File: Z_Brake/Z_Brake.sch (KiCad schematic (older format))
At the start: 29 parts, among them K1 EC2-24NU, K2 EC2-24NU, P1 CONN_01X04, P2 CONN_01X02, P3 CONN_01X04, P4 CONN_01X04, Q1 2N7002, U1 LM397

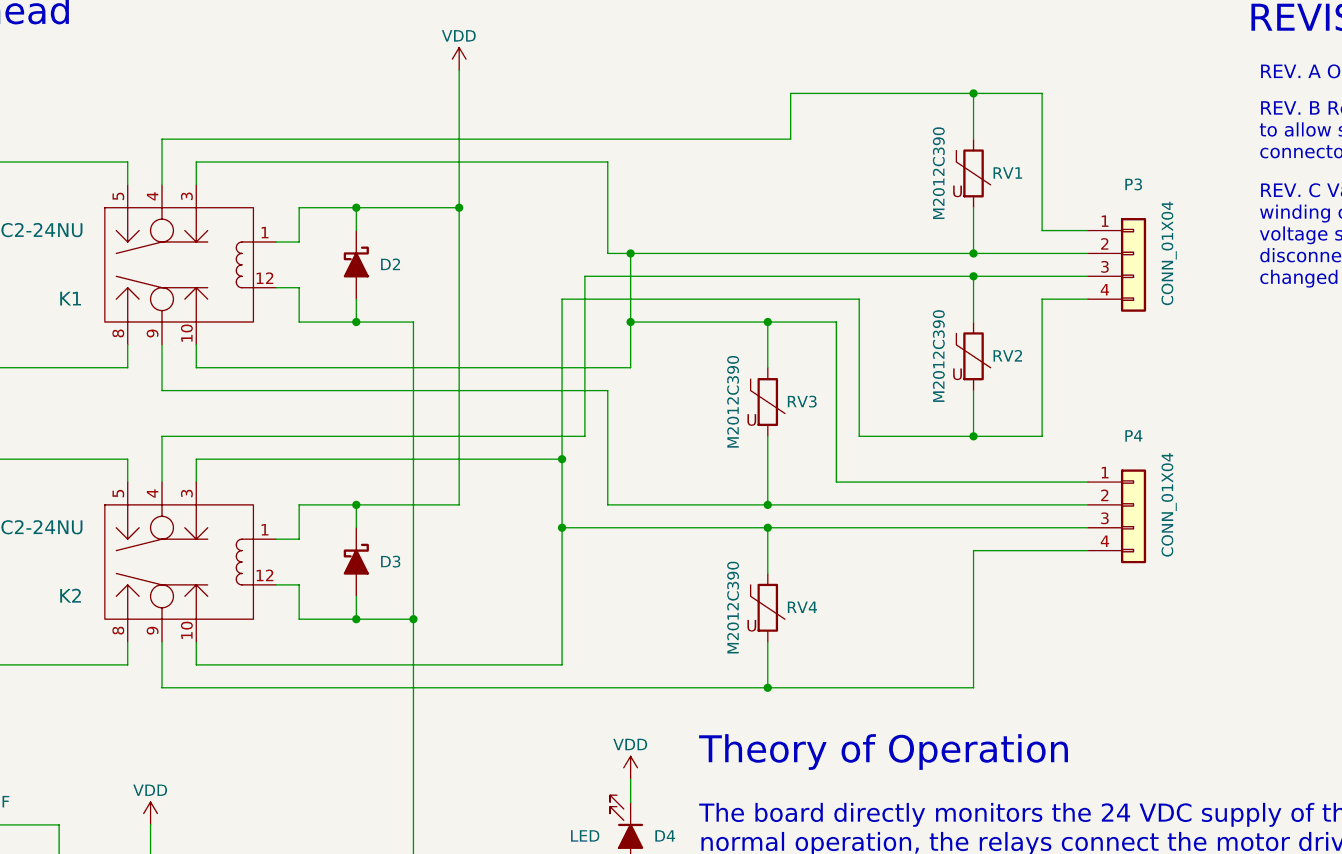
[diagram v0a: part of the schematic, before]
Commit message: Converted to single motor output
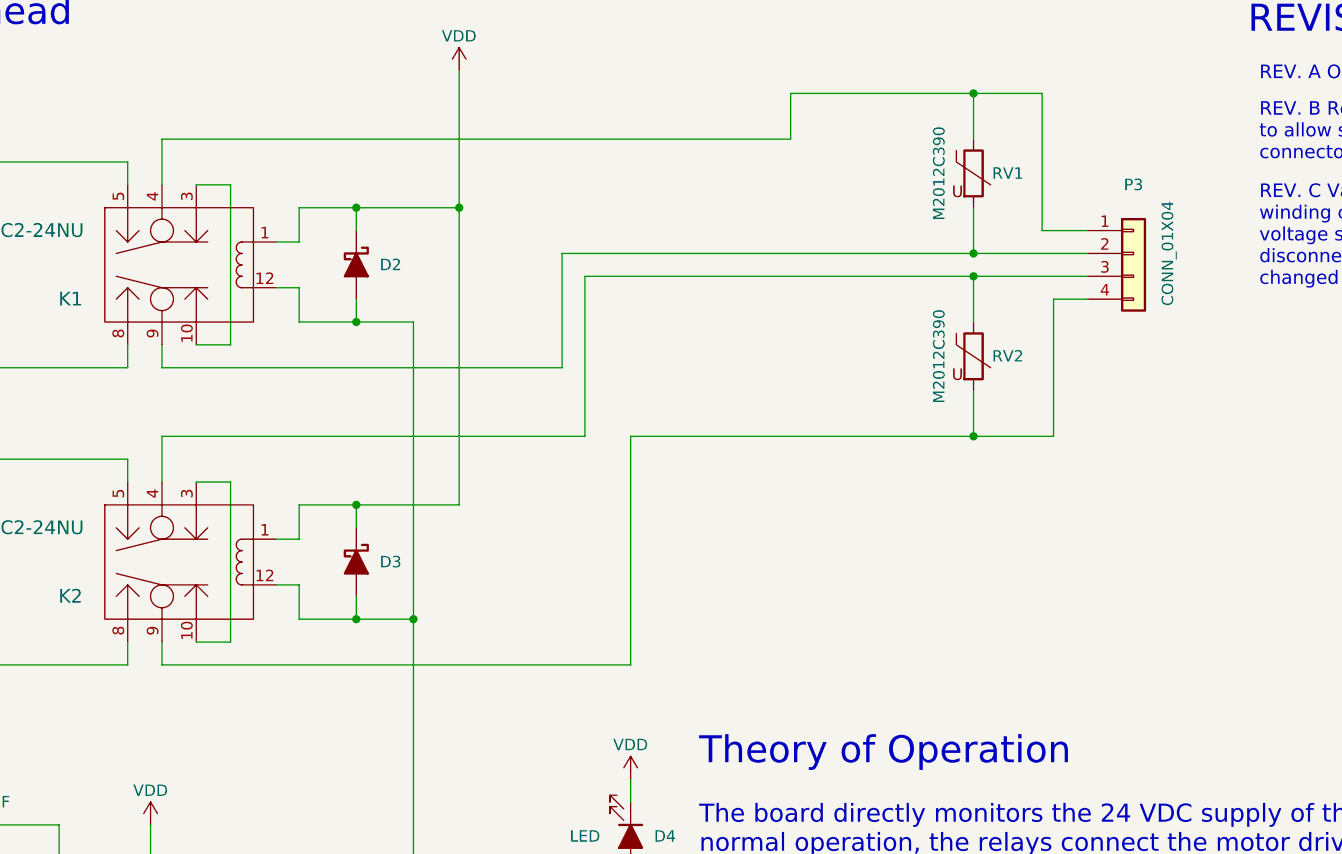
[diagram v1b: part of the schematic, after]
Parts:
- removed P4: CONN_01X04, Pin_Headers:Pin_Header_Straight_1x04, symbol Connector_Generic:Conn_01x04
- removed RV3, RV4: M2012C390, Resistors_SMD:R_0805, symbol Device:Varistor
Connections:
- net at K1.10, K1.3: no longer P3.2 (Pin_2), RV1.2
- net at K1.9: now also P3.2 (Pin_2), RV1.2
- net at K2.10, K2.3: no longer P3.4 (Pin_4), RV2.2
- net at K2.9: now also P3.4 (Pin_4), RV2.2
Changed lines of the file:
@@
-$EndComp
-$Comp
-L ec2-24nu:EC2-24NU K1
-U 1 1 5A25BAB4
-P 4450 1950
-F 0 "K1" H 4050 1800 60  0000 C CNN
-F 1 "EC2-24NU" H 3900 2100 60  0000 C CNN
-F 2 "AO Parts:EC2_Relay" H 4200 1450 60  0001 C CNN
-F 3 "" H 4200 1450 60  0001 C CNN
-F 4 "EC2-24NU" H 4450 1950 60  0001 C CNN "Part Number"
-F 5 "Digikey" H 4450 1950 60  0001 C CNN "Primary Supplier"
-F 6 "399-11037-5-ND" H 4450 1950 60  0001 C CNN "DKPN"
-F 7 "EL-MS-0492" H 4450 1950 60  0001 C CNN "AO Part Number"
-	1    4450 1950
-	1    0    0    -1
 $EndComp
 $Comp
@@
 	1    0    0    -1
 $EndComp
-$Comp
-L Connector_Generic:Conn_01x04 P4
-U 1 1 5A25BDE2
-P 8700 3000
-F 0 "P4" H 8700 3300 50  0000 C CNN
-F 1 "CONN_01X04" V 8850 3000 50  0000 C CNN
-F 2 "Pin_Headers:Pin_Header_Straight_1x04" H 8700 3000 50  0001 C CNN
-F 3 "" H 8700 3000 50  0000 C CNN
-F 4 "WM4802-ND" H 8700 3000 50  0001 C CNN "DKPN"
-	1    8700 3000
-	1    0    0    -1
-$EndComp
 Wire Wire Line
 	4300 1600 4300 1500
@@
 	4450 1400 7200 1400
 Wire Wire Line
-	6400 1900 6400 1500
-Wire Wire Line
-	6400 1500 4600 1500
-Wire Wire Line
-	4600 1500 4600 1600
-Connection ~ 6500 1900
-Wire Wire Line
-	4450 2300 4450 2500
-Wire Wire Line
-	4450 2500 6400 2500
-Wire Wire Line
-	6400 2500 6400 3000
-Wire Wire Line
-	6400 3000 7100 3000
-Wire Wire Line
-	4600 2300 4600 2400
-Wire Wire Line
-	6500 2400 4600 2400
-Wire Wire Line
 	6300 2000 6300 2700
 Wire Wire Line
@@
 Wire Wire Line
 	4450 2700 4450 2900
-Wire Wire Line
-	4450 3600 4450 3800
-Wire Wire Line
-	4450 3800 7100 3800
-Wire Wire Line
-	7100 3800 7100 3600
-Wire Wire Line
-	4600 3600 4600 3700
-Wire Wire Line
-	6200 3700 4600 3700
-Wire Wire Line
-	6200 2100 6200 2800
-Wire Wire Line
-	6200 3100 7100 3100
-Connection ~ 6200 3100
-Wire Wire Line
-	4600 2900 4600 2800
-Wire Wire Line
-	4600 2800 6200 2800
-Connection ~ 6200 2800
 $Comp
 L Device:D_Schottky_ALT D2
@@
 	1    0    0    -1
 $EndComp
-$Comp
-L Device:Varistor RV3
-U 1 1 5B281699
-P 7100 2550
-F 0 "RV3" H 7250 2550 50  0000 C CNN
-F 1 "M2012C390" V 6950 2550 50  0000 C CNN
-F 2 "Resistors_SMD:R_0805" V 7030 2550 50  0001 C CNN
-F 3 "" H 7100 2550 50  0000 C CNN
-F 4 "445-2549-1-ND" H 7100 2550 50  0001 C CNN "DKPN"
-	1    7100 2550
-	1    0    0    -1
-$EndComp
-Connection ~ 7100 3100
-Connection ~ 7100 3000
-$Comp
-L Device:Varistor RV4
-U 1 1 5B281A22
-P 7100 3450
-F 0 "RV4" H 7250 3450 50  0000 C CNN
-F 1 "M2012C390" V 6950 3450 50  0000 C CNN
-F 2 "Resistors_SMD:R_0805" V 7030 3450 50  0001 C CNN
-F 3 "" H 7100 3450 50  0000 C CNN
-F 4 "445-2549-1-ND" H 7100 3450 50  0001 C CNN "DKPN"
-	1    7100 3450
-	1    0    0    -1
-$EndComp
 Wire Wire Line
 	8500 1800 8300 1800
@@
 Connection ~ 8000 1200
 Wire Wire Line
-	6400 1900 6500 1900
-Wire Wire Line
 	8000 1700 8000 1900
-Connection ~ 8000 1900
 Wire Wire Line
 	6300 2000 8000 2000
@@
 Connection ~ 8000 2000
 Wire Wire Line
-	8500 2100 8300 2100
-Wire Wire Line
-	8300 2700 8300 2100
-Wire Wire Line
-	7500 2700 8000 2700
-Wire Wire Line
 	8000 2700 8000 2500
-Wire Wire Line
-	7500 2700 7500 2100
-Wire Wire Line
-	7500 2100 6200 2100
-Connection ~ 8000 2700
-Wire Wire Line
-	8500 2900 7400 2900
-Wire Wire Line
-	7400 2200 7400 2900
-Wire Wire Line
-	6500 2200 7100 2200
-Wire Wire Line
-	7100 2200 7100 2400
-Wire Wire Line
-	6500 1900 6500 2200
-Connection ~ 6500 2200
-Connection ~ 7100 2200
-Wire Wire Line
-	7100 2700 7100 3000
-Wire Wire Line
-	7100 3300 7100 3100
-Wire Wire Line
-	8500 3200 8000 3200
-Wire Wire Line
-	8000 3200 8000 3800
-Connection ~ 7100 3800
 Text Notes 8350 6950 0    118  ~ 0
 Z-BRAKE BOARD
@@
 C
 Wire Wire Line
-	6500 1900 8000 1900
-Wire Wire Line
-	6200 3100 6200 3700
-Wire Wire Line
-	6200 2800 6200 3100
-Wire Wire Line
 	5300 2200 5550 2200
 Wire Wire Line
@@
 	2100 3100 2250 3100
 Wire Wire Line
-	7100 3100 8500 3100
-Wire Wire Line
-	7100 3000 8500 3000
-Wire Wire Line
 	8000 1200 8300 1200
 Wire Wire Line
@@
 Wire Wire Line
 	8000 2000 8500 2000
-Wire Wire Line
-	8000 2700 8300 2700
-Wire Wire Line
-	6500 2200 6500 2400
-Wire Wire Line
-	7100 2200 7400 2200
-Wire Wire Line
-	7100 3800 8000 3800
 $Comp
 L Transistor_FET:2N7002 Q1
@@
 Wire Wire Line
 	5550 5700 5550 6650
+Wire Wire Line
+	2500 5400 2500 6000
+Wire Wire Line
+	2500 5200 2500 5400
+Connection ~ 2500 5400
+Wire Wire Line
+	3200 5400 2500 5400
+Wire Wire Line
+	2900 5600 3200 5600
+Connection ~ 2900 4700
+Wire Wire Line
+	2900 4700 2900 5600
+Connection ~ 2900 5600
+Wire Wire Line
+	1900 5600 1900 6000
+Wire Wire Line
+	1900 5200 1900 5600
+Connection ~ 1900 5600
+Wire Wire Line
+	1900 5600 2900 5600
+$Comp
+L power:VDD #PWR015
+U 1 1 5A6130DB
+P 3500 5150
+F 0 "#PWR015" H 3500 5000 50  0001 C CNN
+F 1 "VDD" H 3500 5300 50  0000 C CNN
+F 2 "" H 3500 5150 50  0000 C CNN
+F 3 "" H 3500 5150 50  0000 C CNN
+	1    3500 5150
+	1    0    0    -1
+$EndComp
+Wire Wire Line
+	3500 5150 3500 5250
+Wire Wire Line
+	3500 5750 3500 5900
+$Comp
+L power:GND #PWR08
+U 1 1 5A28666A
+P 3500 5900
+F 0 "#PWR08" H 3500 5650 50  0001 C CNN
+F 1 "GND" H 3500 5750 50  0000 C CNN
+F 2 "" H 3500 5900 50  0000 C CNN
+F 3 "" H 3500 5900 50  0000 C CNN
+	1    3500 5900
+	1    0    0    -1
+$EndComp
+$Comp
+L lm397:LM397 U1
+U 1 1 5A280FF5
+P 3450 5500
+F 0 "U1" H 3300 5200 60  0000 C CNN
+F 1 "LM397" H 3200 5800 60  0000 C CNN
+F 2 "TO_SOT_Packages_SMD:SOT-23-5" H 3500 5500 60  0001 C CNN
+F 3 "" H 3500 5500 60  0001 C CNN
+F 4 "LM397MF/NOPBCT-ND" H 3450 5500 50  0001 C CNN "DKPN"
+	1    3450 5500
+	1    0    0    -1
+$EndComp
+Wire Wire Line
+	4450 2300 4450 2400
+Wire Wire Line
+	4450 2400 6200 2400
+Wire Wire Line
+	6200 2400 6200 1900
+Wire Wire Line
+	6200 1900 8000 1900
+Connection ~ 8000 1900
+Wire Wire Line
+	4450 3600 4450 3700
+Wire Wire Line
+	4450 3700 6500 3700
+Wire Wire Line
+	6500 3700 6500 2700
+Wire Wire Line
+	6500 2700 8000 2700
+Wire Wire Line
+	8000 2700 8350 2700
+Wire Wire Line
+	8350 2700 8350 2100
+Wire Wire Line
+	8350 2100 8500 2100
+Connection ~ 8000 2700
+Wire Wire Line
+	4750 1600 4750 2300
+Wire Wire Line
+	4750 2900 4750 3600
+Wire Wire Line
+	4750 3600 4600 3600
+Wire Wire Line
+	4600 2900 4750 2900
+Wire Wire Line
+	4750 2300 4600 2300
+Wire Wire Line
+	4600 1600 4750 1600
+$Comp
+L ec2-24nu:EC2-24NU K1
+U 1 1 5A25BAB4
+P 4450 1950
+F 0 "K1" H 4050 1800 60  0000 C CNN
+F 1 "EC2-24NU" H 3900 2100 60  0000 C CNN
+F 2 "AO Parts:EC2_Relay" H 4200 1450 60  0001 C CNN
+F 3 "" H 4200 1450 60  0001 C CNN
+F 4 "EC2-24NU" H 4450 1950 60  0001 C CNN "Part Number"
+F 5 "Digikey" H 4450 1950 60  0001 C CNN "Primary Supplier"
+F 6 "399-11037-5-ND" H 4450 1950 60  0001 C CNN "DKPN"
+F 7 "EL-MS-0492" H 4450 1950 60  0001 C CNN "AO Part Number"
+	1    4450 1950
+	1    0    0    -1
+$EndComp
 $Comp
 L ec2-24nu:EC2-24NU K2
@@
 	1    0    0    -1
 $EndComp
-Wire Wire Line
-	2500 5400 2500 6000
-Wire Wire Line
-	2500 5200 2500 5400
-Connection ~ 2500 5400
-Wire Wire Line
-	3200 5400 2500 5400
-Wire Wire Line
-	2900 5600 3200 5600
-Connection ~ 2900 4700
-Wire Wire Line
-	2900 4700 2900 5600
-Connection ~ 2900 5600
-Wire Wire Line
-	1900 5600 1900 6000
-Wire Wire Line
-	1900 5200 1900 5600
-Connection ~ 1900 5600
-Wire Wire Line
-	1900 5600 2900 5600
-$Comp
-L power:VDD #PWR015
-U 1 1 5A6130DB
-P 3500 5150
-F 0 "#PWR015" H 3500 5000 50  0001 C CNN
-F 1 "VDD" H 3500 5300 50  0000 C CNN
-F 2 "" H 3500 5150 50  0000 C CNN
-F 3 "" H 3500 5150 50  0000 C CNN
-	1    3500 5150
-	1    0    0    -1
-$EndComp
-Wire Wire Line
-	3500 5150 3500 5250
-Wire Wire Line
-	3500 5750 3500 5900
-$Comp
-L power:GND #PWR08
-U 1 1 5A28666A
-P 3500 5900
-F 0 "#PWR08" H 3500 5650 50  0001 C CNN
-F 1 "GND" H 3500 5750 50  0000 C CNN
-F 2 "" H 3500 5900 50  0000 C CNN
-F 3 "" H 3500 5900 50  0000 C CNN
-	1    3500 5900
-	1    0    0    -1
-$EndComp
-$Comp
-L lm397:LM397 U1
-U 1 1 5A280FF5
-P 3450 5500
-F 0 "U1" H 3300 5200 60  0000 C CNN
-F 1 "LM397" H 3200 5800 60  0000 C CNN
-F 2 "TO_SOT_Packages_SMD:SOT-23-5" H 3500 5500 60  0001 C CNN
-F 3 "" H 3500 5500 60  0001 C CNN
-F 4 "LM397MF/NOPBCT-ND" H 3450 5500 50  0001 C CNN "DKPN"
-	1    3450 5500
-	1    0    0    -1
-$EndComp

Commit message: Starting on PCB layout
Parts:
- C1: footprint Capacitors_SMD:C_0603_HandSoldering -> Capacitor_SMD:C_0603_1608Metric_Pad1.08x0.95mm_HandSolder
- D1, D5: footprint Diodes_SMD:SMA_Handsoldering -> Diode_SMD:D_SMA_Handsoldering
- D2, D3: footprint Diodes_SMD:SOD-123 -> Diode_SMD:D_SOD-123
- D4: footprint Capacitors_SMD:C_0603_HandSoldering -> LED_SMD:LED_0603_1608Metric_Pad1.05x0.95mm_HandSolder
- K1: footprint AO Parts:EC2_Relay -> ec2:EC2_Relay; AO Part Number EL-MS-0492 -> (none)
- K2: footprint AO Parts:EC2_Relay -> ec2:EC2_Relay; AO Part Number EL-MS0492 -> (none)
- MH1, MH2, MH3, MH4: footprint AO Parts:MOUNT_HOLE -> MountingHole:MountingHole_2.5mm_Pad
- P1, P3: footprint Pin_Headers:Pin_Header_Straight_1x04 -> Molex:Molex-70543-0038-0-0-MFG
- P2: footprint Pin_Headers:Pin_Header_Straight_1x02 -> Molex:MOLEX_0705430001
- Q1: footprint TO_SOT_Packages_SMD:SOT-23 -> Package_TO_SOT_SMD:SOT-23_Handsoldering
- R1, R2, R3, R4, R5, R6, R7: footprint Resistors_SMD:R_0603_HandSoldering -> Resistor_SMD:R_0603_1608Metric_Pad0.98x0.95mm_HandSolder
- RV1, RV2: footprint Resistors_SMD:R_0805 -> Resistor_SMD:R_0805_2012Metric_Pad1.20x1.40mm_HandSolder
- U1: footprint TO_SOT_Packages_SMD:SOT-23-5 -> Package_TO_SOT_SMD:SOT-23-5_HandSoldering
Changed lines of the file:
@@
 F 0 "C1" V 3350 4200 50  0000 L CNN
 F 1 "0.22uF" V 3350 4500 50  0000 L CNN
-F 2 "Capacitors_SMD:C_0603_HandSoldering" H 3488 4250 50  0001 C CNN
+F 2 "Capacitor_SMD:C_0603_1608Metric_Pad1.08x0.95mm_HandSolder" H 3488 4250 50  0001 C CNN
 F 3 "" H 3450 4400 50  0000 C CNN
 F 4 "1276-6600-1-ND" V 3450 4400 50  0001 C CNN "DKPN"
@@
 F 0 "D1" V 2500 6300 50  0000 C CNN
 F 1 "10.0 V ZENER" H 2500 6000 50  0000 C CNN
-F 2 "Diodes_SMD:SMA_Handsoldering" H 2500 6150 50  0001 C CNN
+F 2 "Diode_SMD:D_SMA_Handsoldering" H 2500 6150 50  0001 C CNN
 F 3 "" H 2500 6150 50  0000 C CNN
 F 4 "SMAZ10-13-F" H 2500 6150 60  0001 C CNN "Part Number"
@@
 F 0 "P1" H 1400 2200 50  0000 C CNN
 F 1 "CONN_01X04" V 1550 1900 50  0000 C CNN
-F 2 "Pin_Headers:Pin_Header_Straight_1x04" H 1400 1900 50  0001 C CNN
+F 2 "Molex:Molex-70543-0038-0-0-MFG" H 1400 1900 50  0001 C CNN
 F 3 "" H 1400 1900 50  0000 C CNN
 F 4 "WM4802-ND" H 1400 1900 50  0001 C CNN "DKPN"
@@
 F 0 "P3" H 8700 2200 50  0000 C CNN
 F 1 "CONN_01X04" V 8850 1900 50  0000 C CNN
-F 2 "Pin_Headers:Pin_Header_Straight_1x04" H 8700 1900 50  0001 C CNN
+F 2 "Molex:Molex-70543-0038-0-0-MFG" H 8700 1900 50  0001 C CNN
 F 3 "" H 8700 1900 50  0000 C CNN
 F 4 "WM4802-ND" H 8700 1900 50  0001 C CNN "DKPN"
@@
 F 0 "D2" V 5300 2100 50  0000 C CNN
 F 1 "D_Schottky_ALT" H 5300 1850 50  0001 C CNN
-F 2 "Diodes_SMD:SOD-123" H 5300 1950 50  0001 C CNN
+F 2 "Diode_SMD:D_SOD-123" H 5300 1950 50  0001 C CNN
 F 3 "" H 5300 1950 50  0000 C CNN
 F 4 "BAT48ZFILM" H 5300 1950 60  0001 C CNN "Part Number"
@@
 F 0 "D3" V 5300 3400 50  0000 C CNN
 F 1 "D_Schottky_ALT" H 5300 3150 50  0001 C CNN
-F 2 "Diodes_SMD:SOD-123" H 5300 3250 50  0001 C CNN
+F 2 "Diode_SMD:D_SOD-123" H 5300 3250 50  0001 C CNN
 F 3 "" H 5300 3250 50  0000 C CNN
 F 4 "BAT48ZFILM" H 5300 3250 60  0001 C CNN "Part Number"
@@
 F 0 "P2" H 1400 3000 50  0000 C CNN
 F 1 "CONN_01X02" V 1550 3200 50  0000 C CNN
-F 2 "Pin_Headers:Pin_Header_Straight_1x02" H 1400 3200 50  0001 C CNN
+F 2 "Molex:MOLEX_0705430001" H 1400 3200 50  0001 C CNN
 F 3 "" H 1400 3200 50  0000 C CNN
 F 4 "WM4800-ND" H 1400 3200 50  0001 C CNN "DKPN"
@@
 F 0 "D4" V 6500 4600 50  0000 C CNN
 F 1 "LED" V 6500 4250 50  0000 C CNN
-F 2 "Capacitors_SMD:C_0603_HandSoldering" H 6500 4450 50  0001 C CNN
+F 2 "LED_SMD:LED_0603_1608Metric_Pad1.05x0.95mm_HandSolder" H 6500 4450 50  0001 C CNN
 F 3 "" H 6500 4450 50  0000 C CNN
 F 4 "160-1184-1-ND" V 6500 4450 50  0001 C CNN "DKPN"
@@
 F 0 "R7" H 6650 4850 50  0000 C CNN
 F 1 "3.3k" H 6350 4850 50  0000 C CNN
-F 2 "Resistors_SMD:R_0603_HandSoldering" V 6430 4850 50  0001 C CNN
+F 2 "Resistor_SMD:R_0603_1608Metric_Pad0.98x0.95mm_HandSolder" V 6430 4850 50  0001 C CNN
 F 3 "" H 6500 4850 50  0000 C CNN
 F 4 "311-3.30KHRCT-ND" H 6500 4850 50  0001 C CNN "DKPN"
@@
 F 0 "R6" V 4930 5500 50  0000 C CNN
 F 1 "10k" V 4750 5500 50  0000 C CNN
-F 2 "Resistors_SMD:R_0603_HandSoldering" V 4780 5500 50  0001 C CNN
+F 2 "Resistor_SMD:R_0603_1608Metric_Pad0.98x0.95mm_HandSolder" V 4780 5500 50  0001 C CNN
 F 3 "" H 4850 5500 50  0000 C CNN
 F 4 "311-10.0KHRCT-ND" V 4850 5500 50  0001 C CNN "DKPN"
@@
 F 0 "R4" V 3530 4700 50  0000 C CNN
 F 1 "180k" V 3350 4700 50  0000 C CNN
-F 2 "Resistors_SMD:R_0603_HandSoldering" V 3380 4700 50  0001 C CNN
+F 2 "Resistor_SMD:R_0603_1608Metric_Pad0.98x0.95mm_HandSolder" V 3380 4700 50  0001 C CNN
 F 3 "" H 3450 4700 50  0001 C CNN
 F 4 "311-180KHRCT-ND" V 3450 4700 50  0001 C CNN "DKPN"
@@
 F 0 "R3" H 2650 5050 50  0000 C CNN
 F 1 "10k" H 2300 5050 50  0000 C CNN
-F 2 "Resistors_SMD:R_0603_HandSoldering" V 2430 5050 50  0001 C CNN
+F 2 "Resistor_SMD:R_0603_1608Metric_Pad0.98x0.95mm_HandSolder" V 2430 5050 50  0001 C CNN
 F 3 "" H 2500 5050 50  0000 C CNN
 F 4 "311-10.0KHRCT-ND" H 2500 5050 50  0001 C CNN "DKPN"
@@
 F 0 "R1" H 2050 5050 50  0000 C CNN
 F 1 "12.4k" H 1700 5050 50  0000 C CNN
-F 2 "Resistors_SMD:R_0603_HandSoldering" V 1830 5050 50  0001 C CNN
+F 2 "Resistor_SMD:R_0603_1608Metric_Pad0.98x0.95mm_HandSolder" V 1830 5050 50  0001 C CNN
 F 3 "" H 1900 5050 50  0000 C CNN
 F 4 "311-12.4KHRCT-ND" H 1900 5050 50  0001 C CNN "DKPN"
@@
 F 0 "R2" H 2050 6150 50  0000 C CNN
 F 1 "10k" H 1700 6150 50  0000 C CNN
-F 2 "Resistors_SMD:R_0603_HandSoldering" V 1830 6150 50  0001 C CNN
+F 2 "Resistor_SMD:R_0603_1608Metric_Pad0.98x0.95mm_HandSolder" V 1830 6150 50  0001 C CNN
 F 3 "" H 1900 6150 50  0000 C CNN
 F 4 "311-10.0KHRCT-ND" H 1900 6150 50  0001 C CNN "DKPN"
@@
 F 0 "R5" H 4550 4950 50  0000 C CNN
 F 1 "10k" H 4250 4950 50  0000 C CNN
-F 2 "Resistors_SMD:R_0603_HandSoldering" V 4330 4950 50  0001 C CNN
+F 2 "Resistor_SMD:R_0603_1608Metric_Pad0.98x0.95mm_HandSolder" V 4330 4950 50  0001 C CNN
 F 3 "" H 4400 4950 50  0000 C CNN
 F 4 "311-10.0KHRCT-ND" H 4400 4950 50  0001 C CNN "DKPN"
@@
 F 0 "MH1" V 7350 6150 50  0000 C CNN
 F 1 "CONN_01X01" V 7350 6150 50  0001 C CNN
-F 2 "AO Parts:MOUNT_HOLE" H 7250 6150 50  0001 C CNN
+F 2 "MountingHole:MountingHole_2.5mm_Pad" H 7250 6150 50  0001 C CNN
 F 3 "" H 7250 6150 50  0000 C CNN
 	1    7250 6150
@@
 F 0 "MH2" V 7750 6150 50  0000 C CNN
 F 1 "CONN_01X01" V 7750 6150 50  0001 C CNN
-F 2 "AO Parts:MOUNT_HOLE" H 7650 6150 50  0001 C CNN
+F 2 "MountingHole:MountingHole_2.5mm_Pad" H 7650 6150 50  0001 C CNN
 F 3 "" H 7650 6150 50  0000 C CNN
 	1    7650 6150
@@
 F 0 "MH3" V 8150 6150 50  0000 C CNN
 F 1 "CONN_01X01" V 8150 6150 50  0001 C CNN
-F 2 "AO Parts:MOUNT_HOLE" H 8050 6150 50  0001 C CNN
+F 2 "MountingHole:MountingHole_2.5mm_Pad" H 8050 6150 50  0001 C CNN
 F 3 "" H 8050 6150 50  0000 C CNN
 	1    8050 6150
@@
 F 0 "MH4" V 8550 6150 50  0000 C CNN
 F 1 "CONN_01X01" V 8550 6150 50  0001 C CNN
-F 2 "AO Parts:MOUNT_HOLE" H 8450 6150 50  0001 C CNN
+F 2 "MountingHole:MountingHole_2.5mm_Pad" H 8450 6150 50  0001 C CNN
 F 3 "" H 8450 6150 50  0000 C CNN
 	1    8450 6150
@@
 F 0 "D5" H 2400 3200 50  0000 C CNN
 F 1 "D_ALT" H 2400 3000 50  0001 C CNN
-F 2 "Diodes_SMD:SMA_Handsoldering" H 2400 3100 50  0001 C CNN
+F 2 "Diode_SMD:D_SMA_Handsoldering" H 2400 3100 50  0001 C CNN
 F 3 "" H 2400 3100 50  0000 C CNN
 F 4 "CDBA340-HF" H 2400 3100 60  0001 C CNN "Part Number"
@@
 F 0 "RV1" H 8150 1550 50  0000 C CNN
 F 1 "M2012C390" V 7850 1550 50  0000 C CNN
-F 2 "Resistors_SMD:R_0805" V 7930 1550 50  0001 C CNN
+F 2 "Resistor_SMD:R_0805_2012Metric_Pad1.20x1.40mm_HandSolder" V 7930 1550 50  0001 C CNN
 F 3 "" H 8000 1550 50  0000 C CNN
 F 4 "445-2549-1-ND" H 8000 1550 50  0001 C CNN "DKPN"
@@
 F 0 "RV2" H 8150 2350 50  0000 C CNN
 F 1 "M2012C390" V 7850 2350 50  0000 C CNN
-F 2 "Resistors_SMD:R_0805" V 7930 2350 50  0001 C CNN
+F 2 "Resistor_SMD:R_0805_2012Metric_Pad1.20x1.40mm_HandSolder" V 7930 2350 50  0001 C CNN
 F 3 "" H 8000 2350 50  0000 C CNN
 F 4 "445-2549-1-ND" H 8000 2350 50  0001 C CNN "DKPN"
@@
 F 0 "Q1" H 5650 5575 50  0000 L CNN
 F 1 "2N7002" H 5650 5500 50  0000 L CNN
-F 2 "TO_SOT_Packages_SMD:SOT-23" H 5650 5425 50  0001 L CIN
+F 2 "Package_TO_SOT_SMD:SOT-23_Handsoldering" H 5650 5425 50  0001 L CIN
 F 3 "" H 5450 5500 50  0000 L CNN
 F 4 "1514-2N7002TRPBFREECT-ND" H 5450 5500 50  0001 C CNN "DKPN"
@@
 F 0 "U1" H 3300 5200 60  0000 C CNN
 F 1 "LM397" H 3200 5800 60  0000 C CNN
-F 2 "TO_SOT_Packages_SMD:SOT-23-5" H 3500 5500 60  0001 C CNN
+F 2 "Package_TO_SOT_SMD:SOT-23-5_HandSoldering" H 3500 5500 60  0001 C CNN
 F 3 "" H 3500 5500 60  0001 C CNN
 F 4 "LM397MF/NOPBCT-ND" H 3450 5500 50  0001 C CNN "DKPN"
@@
 F 0 "K1" H 4050 1800 60  0000 C CNN
 F 1 "EC2-24NU" H 3900 2100 60  0000 C CNN
-F 2 "AO Parts:EC2_Relay" H 4200 1450 60  0001 C CNN
+F 2 "ec2:EC2_Relay" H 4200 1450 60  0001 C CNN
 F 3 "" H 4200 1450 60  0001 C CNN
 F 4 "EC2-24NU" H 4450 1950 60  0001 C CNN "Part Number"
 F 5 "Digikey" H 4450 1950 60  0001 C CNN "Primary Supplier"
 F 6 "399-11037-5-ND" H 4450 1950 60  0001 C CNN "DKPN"
-F 7 "EL-MS-0492" H 4450 1950 60  0001 C CNN "AO Part Number"
 	1    4450 1950
 	1    0    0    -1
@@
 F 0 "K2" H 4050 3100 60  0000 C CNN
 F 1 "EC2-24NU" H 3900 3400 60  0000 C CNN
-F 2 "AO Parts:EC2_Relay" H 4200 2750 60  0001 C CNN
+F 2 "ec2:EC2_Relay" H 4200 2750 60  0001 C CNN
 F 3 "" H 4200 2750 60  0001 C CNN
 F 4 "EC2-24NU" H 4450 3250 60  0001 C CNN "Part Number"
 F 5 "Digikey" H 4450 3250 60  0001 C CNN "Primary Supplier"
 F 6 "399-11037-5-ND" H 4450 3250 60  0001 C CNN "DKPN"
-F 7 "EL-MS0492" H 4450 3250 60  0001 C CNN "AO Part Number"
 	1    4450 3250
 	1    0    0    -1
